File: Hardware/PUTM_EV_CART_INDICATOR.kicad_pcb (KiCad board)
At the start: 2 copper layers, 43 x 27 mm, 19 parts, among them J1 Screw_Terminal_01x08, K3 IM07DTS, K4 IM07DTS

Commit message: Wersja 2.0 do sprawdzenia :3
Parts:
- removed D1: D, Diode_SMD:D_0603_1608Metric_Pad1.05x0.95mm_HandSolder
- removed the H1 at (122.0, 80.0)
- removed the H1 at (85.0, 80.0)
- removed the H2 at (122.0, 74.0)
- removed the H2 at (85.0, 74.0)
- removed R12: 1K, Resistor_SMD:R_0603_1608Metric_Pad0.98x0.95mm_HandSolder
- added C1: NC, Capacitor_SMD:C_0603_1608Metric_Pad1.08x0.95mm_HandSolder, F.Cu at (152.8, 67.2)
- added C2: NC, Capacitor_SMD:C_0603_1608Metric_Pad1.08x0.95mm_HandSolder, F.Cu at (181.2, 66.5)
- added D5: D, Diode_SMD:Nexperia_CFP3_SOD-123W, F.Cu at (159.2, 50.3)
- added D6: D, Diode_SMD:Nexperia_CFP3_SOD-123W, F.Cu at (174.2, 68.0)
- added F1: 1.5A PPTC fuse, Library:Fuse_2920_7451Metric_Pad2.10x5.45mm_HandSolder, F.Cu at (174.0, 53.0)
- added H1: MountingHole, MountingHole:MountingHole_2.2mm_M2, F.Cu at (148.5, 70.2)
- added H2: MountingHole, MountingHole:MountingHole_2.2mm_M2, F.Cu at (186.2, 50.2)
- added H3: MountingHole, MountingHole:MountingHole_2.2mm_M2, F.Cu at (184.0, 70.0)
- added H4: MountingHole, MountingHole:MountingHole_2.2mm_M2, F.Cu at (146.8, 50.5)
- added JP1: Jumper_2_Open, Jumper:SolderJumper-2_P1.3mm_Open_RoundedPad1.0x1.5mm, B.Cu at (166.5, 51.5)
- added Q1: PMOS, Package_TO_SOT_SMD:SOT-223, F.Cu at (166.2, 52.2)
- added R1: R_Small, Resistor_SMD:R_0603_1608Metric_Pad0.98x0.95mm_HandSolder, F.Cu at (157.0, 50.7)
- added R13: NC, Resistor_SMD:R_0603_1608Metric_Pad0.98x0.95mm_HandSolder, F.Cu at (181.5, 50.8)
- added R14: NC, Resistor_SMD:R_0603_1608Metric_Pad0.98x0.95mm_HandSolder, F.Cu at (152.6, 57.0)
- added R15: NC, Resistor_SMD:R_0603_1608Metric_Pad0.98x0.95mm_HandSolder, F.Cu at (152.4, 50.5)
- added U1: 30mA const current led driver, Include:DIO_1-13_DIO-L, F.Cu at (181.5, 55.2)
- added U2: 30mA const current led driver, Include:DIO_1-13_DIO-L, F.Cu at (181.5, 52.8)
- added U3: 30mA const current led driver, Include:DIO_1-13_DIO-L, F.Cu at (152.5, 55.0)
- added U4: 30mA const current led driver, Include:DIO_1-13_DIO-L, F.Cu at (152.5, 52.8)
- D2: footprint Diode_SMD:D_0603_1608Metric_Pad1.05x0.95mm_HandSolder -> Diode_SMD:Nexperia_CFP3_SOD-123W
- R11: value 1K -> NC
- moved R11 71.5 mm to (181.2, 57.2), turned to 0 degrees
- moved D3 67.8 mm to (157.2, 72.0), turned to 180 degrees
- moved J1 67.2 mm to (149.0, 41.8)
- moved R22 66.4 mm to (181.2, 60.8), turned to 180 degrees
- moved K4 66.1 mm to (172.8, 62.2), turned to 180 degrees
- moved Q4 65.6 mm to (181.2, 63.8)
- moved R10 64.7 mm to (181.2, 59.2), turned to 180 degrees
- moved R8 64.5 mm to (152.5, 59.2), turned to 0 degrees
- moved K3 64.0 mm to (160.7, 62.2), turned to 180 degrees
- moved Q5 63.4 mm to (152.5, 63.8)
- moved D2 62.4 mm to (161.2, 67.8)
- moved R6 62.2 mm to (152.5, 60.8), turned to 180 degrees
- moved D4 59.0 mm to (174.8, 72.0), turned to 0 degrees
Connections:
- net Net-(K4-NC_2) renamed /current_driver/Input
- D2 pad 1: +24V -> /24V_fused
- D3 pad 2: /TSAL_LED -> /current_driver2/Output
- D4 pad 2: /IMD_LED -> /current_driver/Output
- K3 pad 1: +24V -> /24V_fused
- K3 pad 3: +24V -> /24V_fused
- K3 pad 4: Net-(K3-NO_1) -> /current_driver2/Input
- K3 pad 6: +24V -> /24V_fused
- K4 pad 1: +24V -> /24V_fused
- K4 pad 3: +24V -> /24V_fused
- K4 pad 6: +24V -> /24V_fused
- R11 pad 1: /IMD_LED -> /current_driver/Output
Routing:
- net /24V_fused: track 0.00 -> 58.0 mm, vias 0 -> 1
- net +24V: track 54.2 -> 16.5 mm, vias 0 -> 1
- net /current_driver2/Output: track 0.00 -> 21.8 mm, vias 0 -> 2
- net /TSAL_GREEN: track 9.76 -> 29.9 mm
- net /current_driver/Output: track 0.00 -> 19.5 mm, vias 0 -> 2
- net Net-(D5-K): track 0.00 -> 18.0 mm
- net /current_driver/Input: track 6.36 -> 22.0 mm, vias 0 -> 2
- net /current_driver2/Input: track 0.00 -> 13.7 mm
- net /TSAL_LED: track 25.8 -> 12.4 mm
- net Net-(D5-A): track 0.00 -> 9.17 mm, vias 0 -> 2
- net /IMD_LED: track 20.2 -> 11.9 mm
- net GND: track 0.00 -> 6.88 mm, vias 4 -> 9
- net /TSAL_COLUMN: track 29.4 -> 36.2 mm
- net /IMD: track 15.6 -> 21.1 mm
- net Net-(Q5-G): track 4.97 -> 8.61 mm
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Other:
- board size 43 x 27 mm -> 45 x 38.8 mm
- board text added: "IMD ERROR"
- board text removed: "IMD"
- board text removed: "Krzysiu Ch*** faktury oddawaj"

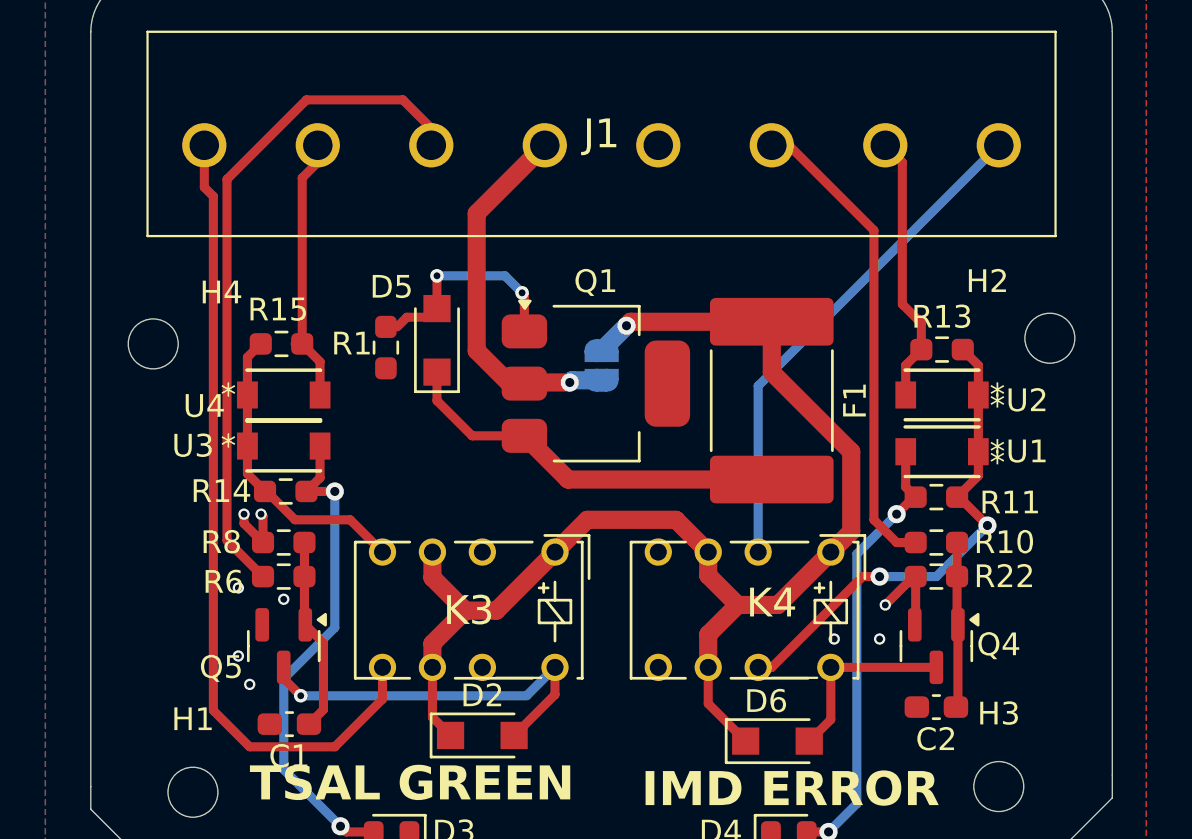
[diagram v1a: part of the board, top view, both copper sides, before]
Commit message: Dodano esd protection, zmieniono komponenty, poprawiono schemat itp
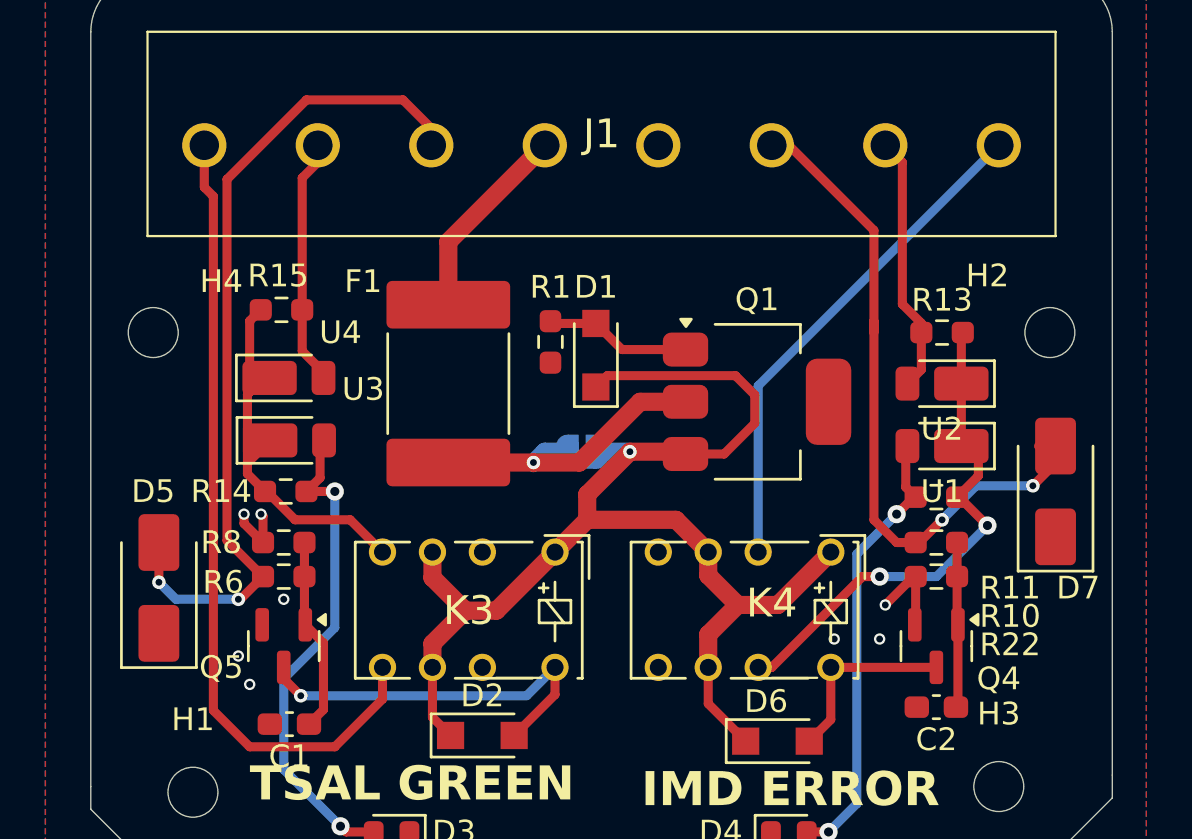
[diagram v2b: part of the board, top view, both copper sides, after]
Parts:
- added D1: D_Schottky, Diode_SMD:Nexperia_CFP3_SOD-123W, F.Cu at (166.2, 51.0)
- added D7: D_TVS, Diode_SMD:D_SMA, F.Cu at (186.5, 57.0)
- D3: value LED -> GREEN LED
- D4: value LED -> RED LED
- D5: value D -> D_TVS; footprint Diode_SMD:Nexperia_CFP3_SOD-123W -> Diode_SMD:D_SMA
- Q1: value PMOS -> 70V 2.4A PMOS
- R1: value R_Small -> 100k
- U1, U2, U3, U4: footprint Include:DIO_1-13_DIO-L -> Diode_SMD:D_PowerDI-123
- moved D5 16.4 mm to (147.0, 61.2)
- moved F1 14.3 mm to (159.8, 52.2), turned to 90 degrees
- moved R1 7.25 mm to (164.2, 50.4)
- moved Q1 7.14 mm to (173.3, 53.0)
- moved JP1 3.89 mm to (165.7, 55.2), turned to 0 degrees
- moved R15 1.50 mm to (152.4, 49.0)
- moved U4 0.78 mm to (152.7, 52.0)
- moved R13 0.75 mm to (181.5, 50.0)
- moved H4 0.50 mm to (146.8, 50.0)
- moved U2 0.50 mm to (181.5, 52.2)
- moved U3 0.35 mm to (152.8, 54.8)
- moved H2 0.25 mm to (186.2, 50.0)
- moved U1 0.25 mm to (181.5, 55.0)
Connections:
- D5 pad 1: Net-(D5-K) -> GND
- D5 pad 2: Net-(D5-A) -> /TSAL_GREEN
- F1 pad 1: /24V_fused -> Net-(JP1-A)
- F1 pad 2: Net-(D5-K) -> +24V
- JP1 pad 1: +24V -> Net-(JP1-A)
- Q1 pad 1: Net-(D5-A) -> Net-(D1-A)
- Q1 pad 2: +24V -> Net-(JP1-A)
- Q1 pad 3: Net-(D5-K) -> /24V_fused
- R1 pad 1: Net-(D5-A) -> Net-(D1-A)
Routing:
- net Net-(D5-K): track 18.0 -> 0.00 mm
- net Net-(JP1-A): track 0.00 -> 13.4 mm, vias 0 -> 1
- net /IMD: track 21.1 -> 30.7 mm, vias 0 -> 2
- net Net-(D5-A): track 9.17 -> 0.00 mm, vias 2 -> 0
- net +24V: track 16.5 -> 8.79 mm, vias 1 -> 0
- net /TSAL_GREEN: track 29.9 -> 36.9 mm, vias 0 -> 2
- net Net-(D1-A): track 0.00 -> 6.47 mm
- net /current_driver2/Input: track 13.7 -> 18.0 mm
- net /TSAL_LED: track 12.4 -> 11.0 mm
- net /IMD_LED: track 11.9 -> 11.4 mm
- net GND: vias 9 -> 8

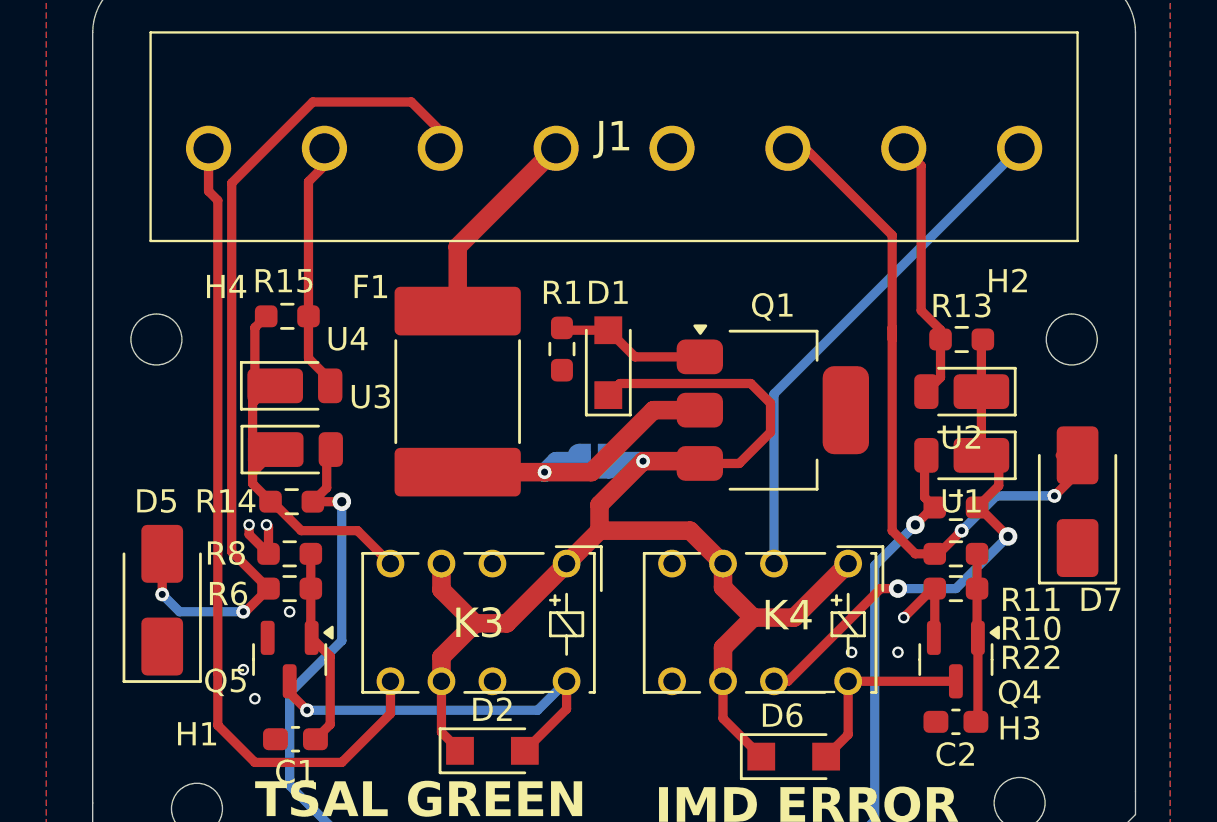
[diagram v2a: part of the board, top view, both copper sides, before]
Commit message: Dodano TVS na kazde wejscie, zmieniono diode w reverse polarity protection na zenera
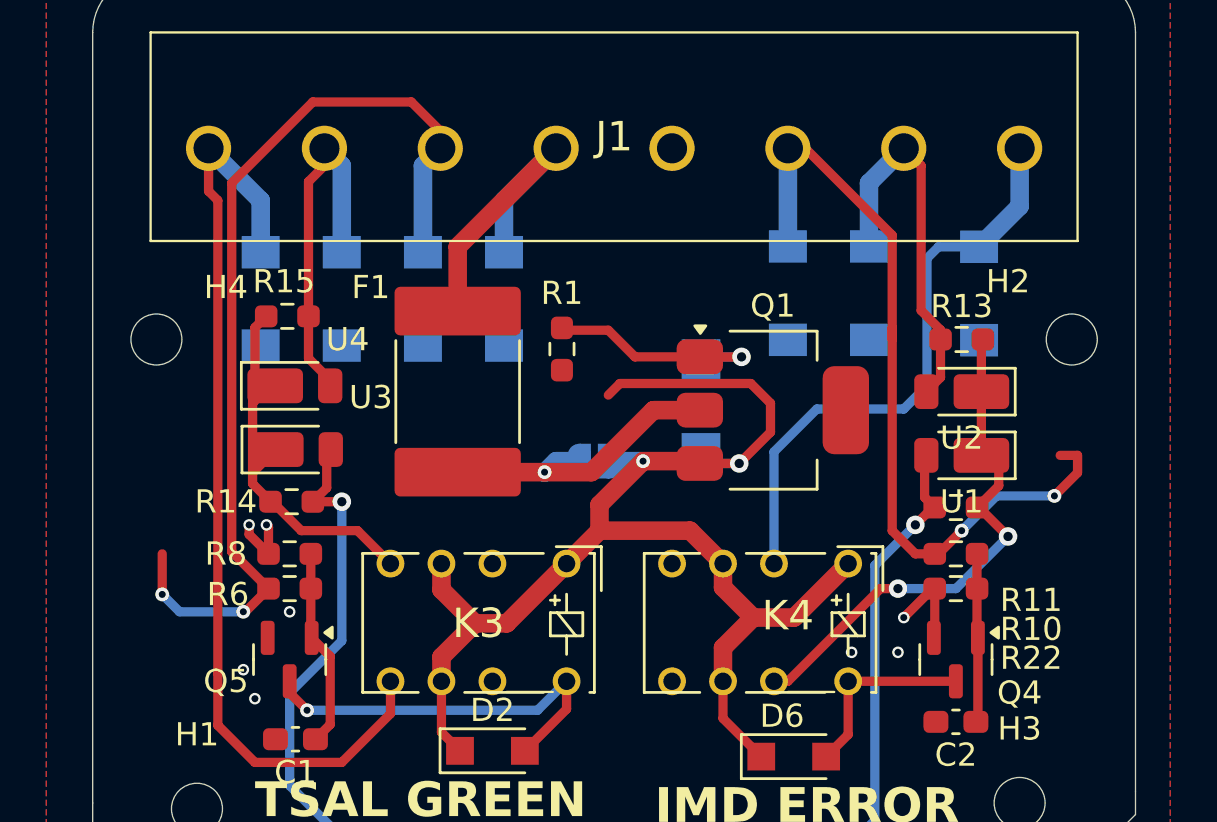
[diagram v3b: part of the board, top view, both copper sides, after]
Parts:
- removed D1: D_Schottky, Diode_SMD:Nexperia_CFP3_SOD-123W
- removed D5, D7: D_TVS, Diode_SMD:D_SMA
- added D10: D_TVS, Include:SM4T82AY, B.Cu at (154.8, 48.2)
- added D11: D_TVS, Include:SM4T82AY, B.Cu at (177.5, 48.0)
- added D12: D_TVS, Include:SM4T82AY, B.Cu at (182.2, 48.0)
- added D13: D_TVS, Include:SM4T82AY, B.Cu at (174.0, 48.0)
- added D14: D_TVS, Include:SM4T82AY, B.Cu at (158.2, 48.2)
- added D15: D_TVS, Include:SM4T82AY, B.Cu at (161.8, 48.2)
- added D8: D_Zener, Include:SODFL5026X125N, B.Cu at (170.2, 53.0)
- added D9: D_TVS, Include:SM4T82AY, B.Cu at (151.2, 48.2)
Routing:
- net /TSAL_COLUMN: track 36.2 -> 41.6 mm
- net +24V: track 8.79 -> 14.2 mm
- net /IMD_LED: track 11.4 -> 16.3 mm
- net /TSAL_GREEN: track 36.9 -> 41.7 mm
- net /TSAL_LED: track 11.0 -> 15.8 mm
- net /IMD: track 30.7 -> 34.9 mm
- net Net-(D8-A): track 6.47 -> 10.1 mm, vias 0 -> 1
- net /IMD_COLUMN: track 22.3 -> 25.5 mm
- net /24V_fused: track 58.3 -> 60.1 mm, vias 1 -> 2
